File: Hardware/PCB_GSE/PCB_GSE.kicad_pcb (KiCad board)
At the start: 4 copper layers, 74 x 95.6 mm, 154 parts, among them J1 Conn_01x06_Pin, J2 Vin_XT30PW-F, J3 Screw_Terminal_01x06, J4 GT17HN-4DP-2H(D)(56), J6 Conn_01x02, J7 Screw_Terminal_01x04, J8 Screw_Terminal_01x04, U1 STM32F103CBT6, U10 INA125UA/2K5, U11 MAX6612MXK, U2 MPQ9843GLE-5-AEC1-Z, U3 MP28167GQ-B-P, U4 TLV75733PDBVR, U5 SI5442DU-T1-GE3, U6 SI5442DU-T1-GE3, U7 SI5442DU-T1-GE3, U8 ISOW1044, U9 INA125UA/2K5

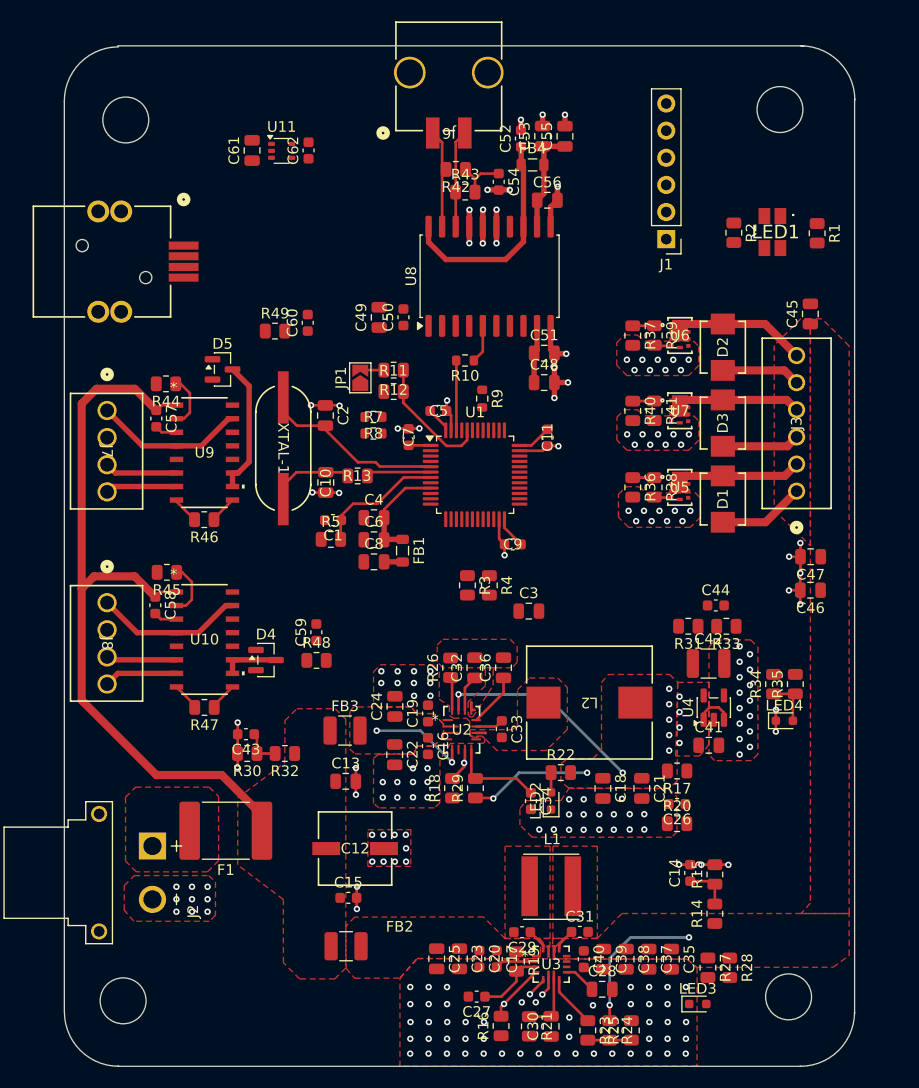
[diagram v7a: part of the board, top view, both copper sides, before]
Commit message: fix(gse & moteur): mapping + routing, remove CAN_ISO_IN/OUT
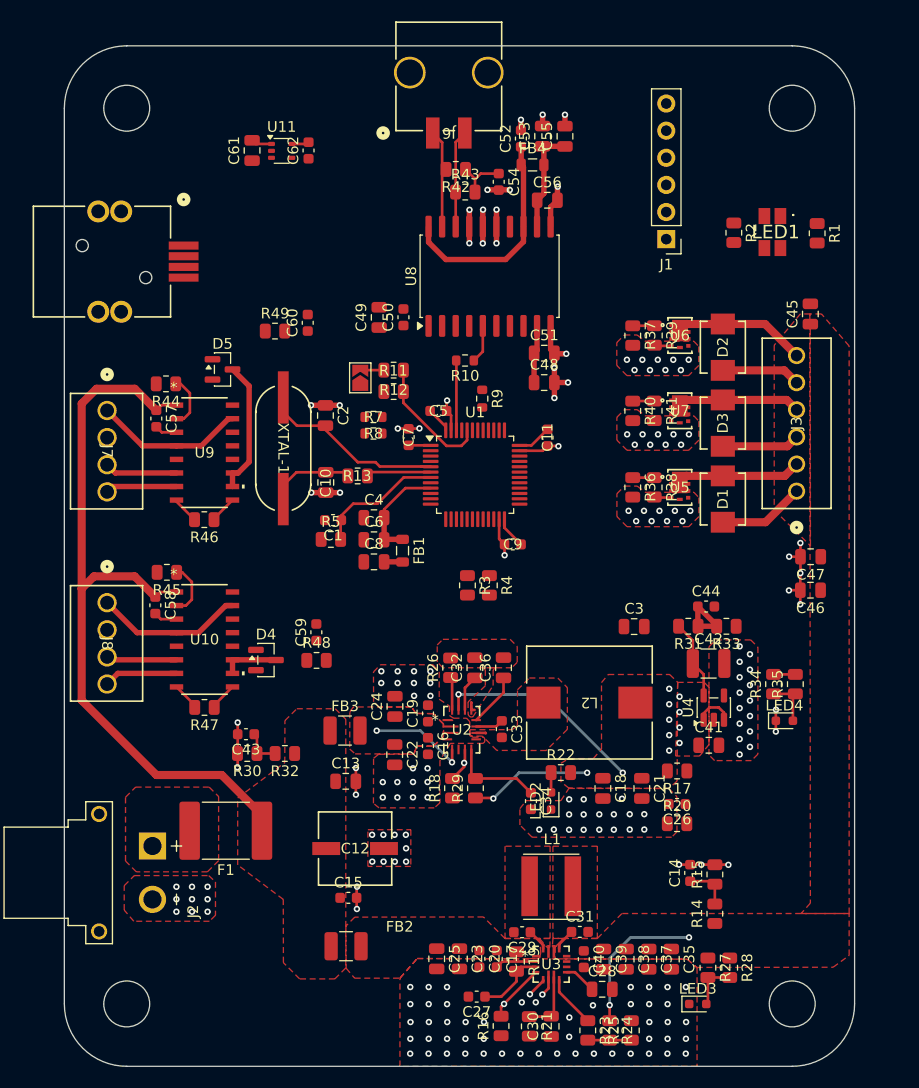
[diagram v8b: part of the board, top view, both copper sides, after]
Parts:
- moved C3 9.97 mm to (168.1, 108.0)
- moved H1 1.15 mm to (182.9, 59.4)
- moved H2 1.11 mm to (120.6, 59.4)
- moved C44 0.92 mm to (174.9, 106.1)
- moved H4 0.74 mm to (182.9, 143.3)
- moved H3 0.44 mm to (120.6, 143.3)
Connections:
- U1 pad 13: 12V_An -> Vin_An
- U1 pad 14: 5V_An -> 12V_An
- U1 pad 15: 3V3_An -> Power_Good_12V
- U1 pad 16: Vin_An -> unconnected-(U1-PA6-Pad16)
- U1 pad 17: Power_Good_5V -> 5V_An
- U1 pad 18: CriticalLED_G -> Power_Good_5V
- U1 pad 19: CriticalLED_R -> 3V3_An
- U1 pad 20: EXTEND_IO3 -> unconnected-(U1-PB2-Pad20)
- U1 pad 25: Power_Good_12V -> CriticalLED_R
- U1 pad 26: EXTEND_IO5 -> CriticalLED_G
- U1 pad 27: EXTEND_IO6 -> unconnected-(U1-PB14-Pad27)
- U1 pad 28: EXTEND_IO7 -> unconnected-(U1-PB15-Pad28)
- U1 pad 29: EXTEND_IO8 -> unconnected-(U1-PA8-Pad29)
- U1 pad 30: EXTEND_IO9 -> unconnected-(U1-PA9-Pad30)
- U1 pad 38: EXTEND_IO10 -> unconnected-(U1-PA15-Pad38)
- U1 pad 40: EXTEND_IO11 -> unconnected-(U1-PB4-Pad40)
- U1 pad 41: EXTEND_IO12 -> unconnected-(U1-PB5-Pad41)
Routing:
- net 3V_Main: track 18.0 -> 27.5 mm
- net 3V3_An: track 0.00 -> 6.18 mm
- net Net-(LED3-A): track 0.00 -> 4.58 mm
- net GND: track 59.6 -> 63.4 mm
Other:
- outline, holes or cut-outs redrawn
